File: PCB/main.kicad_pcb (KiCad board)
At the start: 2 copper layers, 112.9 x 63.7 mm, 105 parts, among them K1 HK19F-DCxxV-SHC, Q10 BC817, Q11 BC817, Q12 TPCA8120,L1Q, Q13 BC817, Q14 BC817, Q15 BC817, Q16 TPCA8120,L1Q, Q17 BC817, Q18 TPCA8120,L1Q, Q19 BC817, Q2 BC817, Q3 TPCA8120,L1Q, Q4 BC817, Q5 TPCA8120,L1Q, Q6 TPCA8120,L1Q, Q7 TPCA8120,L1Q, Q8 BC817, Q9 BC817, SW1 config, U1 ESP32-S2-DevKitM, U2 L7805

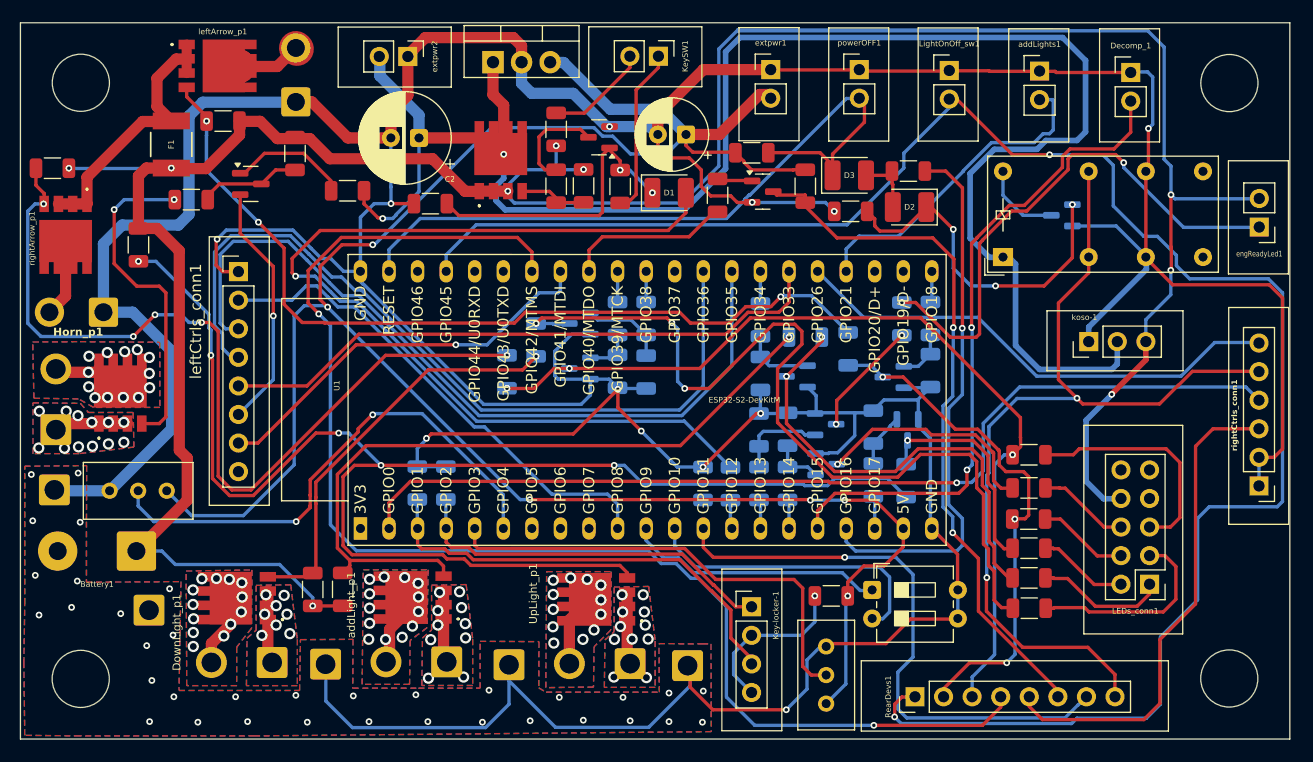
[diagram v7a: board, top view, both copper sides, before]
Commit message: Many fixes and changes
- Electric schema and PCB changes:
	- To avoid unwanted service starting (lights, electric start engine....), the signals from the motorbike's front side to
	  the rear one, are no more connedted to the FET's gate directly. There is a second stage realized with PNPs transistors,
	  now. It is a more stable and safe solution.

- In the shcema:
	- All the c_<signal> symbols have been splitted in ci_<signal> and co_<signal>, and the symbols direction (input/output)
	  have been fixed
	- To get a more readable schema, the c*_<signal> symbols have a different color
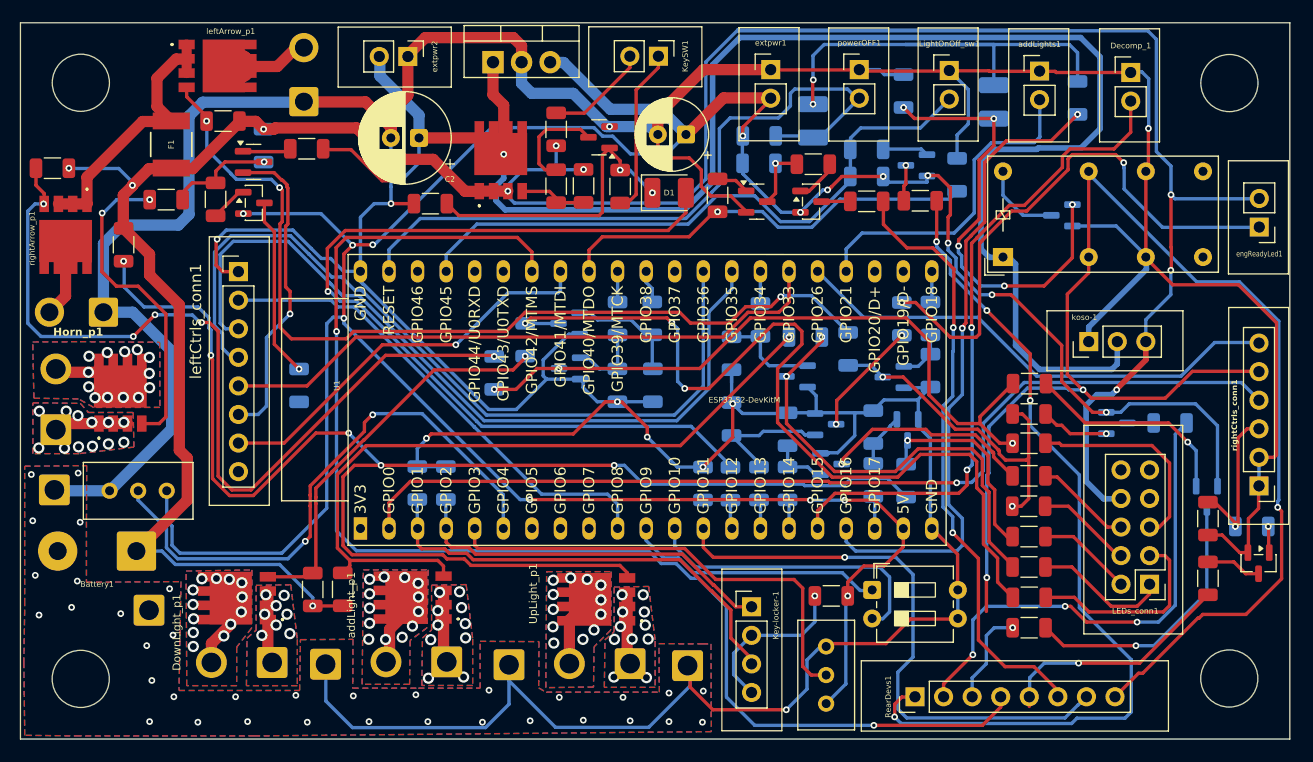
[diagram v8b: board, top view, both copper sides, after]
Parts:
- added Q1: BC807, Package_TO_SOT_SMD:SOT-23, B.Cu at (151.7, 89.3)
- added Q20: BC807, Package_TO_SOT_SMD:SOT-23, B.Cu at (159.7, 95.9)
- added Q21: BC807, Package_TO_SOT_SMD:SOT-23, F.Cu at (75.0, 69.7)
- added Q22: BC807, Package_TO_SOT_SMD:SOT-23, B.Cu at (133.9, 66.4)
- added Q23: BC807, Package_TO_SOT_SMD:SOT-23, F.Cu at (124.5, 69.6)
- added Q24: BC807, Package_TO_SOT_SMD:SOT-23, F.Cu at (164.3, 101.8)
- added R14: 100K, Resistor_SMD:R_1206_3216Metric, B.Cu at (137.5, 67.2)
- added RA37: 10K, Resistor_SMD:R_1206_3216Metric, F.Cu at (143.9, 88.5)
- added RA38: 10K, Resistor_SMD:R_1206_3216Metric, F.Cu at (143.9, 85.8)
- added RA39: 10K, Resistor_SMD:R_1206_3216Metric, F.Cu at (71.6, 69.4)
- added RA40: 10K, Resistor_SMD:R_1206_3216Metric, B.Cu at (163.7, 98.5)
- added RA41: 100K, Resistor_SMD:R_1206_3216Metric, F.Cu at (159.8, 97.8)
- added RA42: 1K, Resistor_SMD:R_1206_3216Metric, F.Cu at (159.8, 103.1)
- added RA43: 1K, Resistor_SMD:R_1206_3216Metric, B.Cu at (156.4, 89.3)
- added RA44: 1K, Resistor_SMD:R_1206_3216Metric, F.Cu at (143.9, 107.5)
- added RA45: 1K, Resistor_SMD:R_1206_3216Metric, B.Cu at (79.0, 86.0)
- added RA46: 10K, Resistor_SMD:R_1206_3216Metric, B.Cu at (129.5, 65.0)
- added RA47: 100K, Resistor_SMD:R_1206_3216Metric, B.Cu at (129.5, 67.4)
- added RA48: 1K, Resistor_SMD:R_1206_3216Metric, F.Cu at (134.2, 69.5)
- added RA49: 10K, Resistor_SMD:R_1206_3216Metric, F.Cu at (124.7, 66.3)
- added RA51: 1K, Resistor_SMD:R_1206_3216Metric, F.Cu at (129.5, 69.6)
- D2, D3, R1, R5, RA1, RA2, RA21: moved to B.Cu
- moved RA2 16.4 mm to (148.2, 60.4), turned to 90 degrees
- moved D2 12.0 mm to (140.8, 60.8), turned to 90 degrees
- moved RA1 11.7 mm to (132.7, 59.8), turned to -90 degrees
- moved D3 5.82 mm to (124.7, 62.4), turned to 90 degrees
- moved RA29 5.21 mm to (79.7, 64.9)
- moved R5 4.59 mm to (119.9, 66.2), turned to 0 degrees
- moved RA20 3.13 mm to (117.5, 83.1)
- moved RA21 2.88 mm to (75.8, 64.6)
- moved RA28 2.62 mm to (117.5, 89.0)
- moved RA26 2.24 mm to (67.2, 69.4)
- moved Q17 1.97 mm to (75.0, 66.1)
- moved R1 1.64 mm to (119.9, 63.8)
- moved RA23 1.32 mm to (110.5, 86.0)
- moved RA10 1.32 mm to (63.4, 73.5)
- moved RA25 1.24 mm to (107.3, 86.0)
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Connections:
- net c_engineOFF renamed ci_engineOFF
- net c_horn renamed ci_horn
- LightOnOff_sw1 pad 2: c_rearLight -> i_lightON/OFF
- Q11 pad 3: c_leftArrow -> Net-(Q11-C)
- Q13 pad 3: c_rightArrow -> Net-(Q13-C)
- Q19 pad 3: c_startEngine -> Net-(Q19-C)
- R5 pad 1: c_startEngine -> 5V
- R5 pad 2: 5V -> Net-(Q19-C)
- RA1 pad 1: Net-(D2-K) -> GND
- RA1 pad 2: GND -> Net-(D2-K)
- RA18 pad 1: c_leftArrow -> Net-(Q11-C)
- RA19 pad 1: c_rightArrow -> Net-(Q13-C)
- RA6 pad 1: c_leftArrow -> Net-(Q11-C)
- RA7 pad 1: c_rightArrow -> Net-(Q13-C)
- RearDevs1 pad 1: c_rearLight -> co_rearLight
- RearDevs1 pad 2: c_leftArrow -> co_leftArrow
- RearDevs1 pad 3: c_rightArrow -> co_rightArrow
- RearDevs1 pad 5: c_brakeSwitch -> co_brakeSwitch
- RearDevs1 pad 6: c_startEngine -> co_startEngine
- U1 pad 39: c_rearLight -> i_lightON/OFF
- rightCtrls_conn1 pad 3: c_brakeSwitch -> ci_brakeSwitch
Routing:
- net c_rearLight: track 165.0 -> 0.00 mm, vias 2 -> 0
- net 5V: track 189.1 -> 268.1 mm, vias 6 -> 16
- net c_rightArrow: track 78.9 -> 0.00 mm, vias 3 -> 0
- net co_rearLight: track 0.00 -> 77.5 mm, vias 0 -> 4
- net c_startEngine: track 63.3 -> 0.00 mm, vias 2 -> 0
- net Net-(Q13-C): track 0.00 -> 61.2 mm, vias 0 -> 3
- net i_lightON/OFF: track 0.00 -> 56.8 mm
- net co_startEngine: track 0.00 -> 54.9 mm, vias 0 -> 2
- net ci_engineOFF: track 80.7 -> 129.3 mm, vias 2 -> 3
- net c_leftArrow: track 46.5 -> 0.00 mm, vias 3 -> 0
- net co_leftArrow: track 0.00 -> 44.2 mm, vias 0 -> 3
- net c_brakeSwitch: track 44.0 -> 0.00 mm
- net Net-(D2-A): track 5.70 -> 42.6 mm, vias 0 -> 2
- net Net-(Q11-C): track 0.00 -> 30.2 mm, vias 0 -> 2
- net Net-(Q20-C): track 0.00 -> 24.5 mm, vias 0 -> 1
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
